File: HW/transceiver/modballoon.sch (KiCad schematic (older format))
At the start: 15 parts, among them K1 CONN_6, K2 CONN_10, K3 CONN_6, K4 CONN_6, K5 SMA, K6 SMA, K7 HE10-20

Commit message: PCB of transceiver designed.
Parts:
- added M1, M2, M3, M4: CONN_01X01, Balloln_pretty:M2, symbol CONN_01X01
- added M5, M6, M7, M8: CONN_01X01, Balloln_pretty:M3, symbol CONN_01X01
- added S1: BMI-S-210-F, Balloln_pretty:BMI-S-210-F, symbol CONN_01X24
- C1, C2: footprint ~ -> Capacitors_SMD:C_0603; symbol C -> C-RESCUE-modballoon
- DD1: footprint ~ -> TO_SOT_Packages_SMD:SC-70-5
- F1: footprint 0603 -> Resistors_SMD:R_0603
- K1, K3, K4: footprint (none) -> Pin_Headers:Pin_Header_Straight_1x06
- K2: footprint (none) -> Pin_Headers:Pin_Header_Straight_1x10
- K5, K6: footprint ~ -> Balloln_pretty:SMA
- K7: footprint (none) -> Pin_Headers:Pin_Header_Straight_2x10
- L1: footprint ~ -> Capacitors_SMD:C_0805
- R1, R2, R3: footprint ~ -> Resistors_SMD:R_0603; symbol R -> R-RESCUE-modballoon
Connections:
- net GND: now also M1.1 (P1), M2.1 (P1), M3.1 (P1), M4.1 (P1), M5.1 (P1), M6.1 (P1), M7.1 (P1), M8.1 (P1), S1.1 (P1), S1.10 (P10), S1.11 (P11), S1.12 (P12), S1.13 (P13), S1.14 (P14), S1.15 (P15), S1.16 (P16), S1.17 (P17), S1.18 (P18), S1.19 (P19), S1.2 (P2), S1.20 (P20), S1.21 (P21), S1.22 (P22), S1.23 (P23), S1.24 (P24), S1.3 (P3), S1.4 (P4), S1.5 (P5), S1.6 (P6), S1.7 (P7), S1.8 (P8), S1.9 (P9)

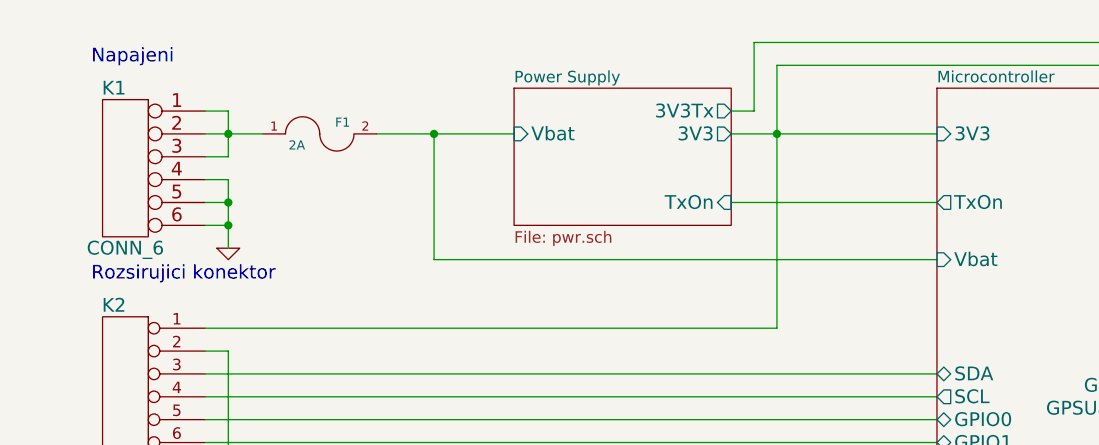
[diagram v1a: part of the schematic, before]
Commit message: new protection feature - inverted power supply protection diode.
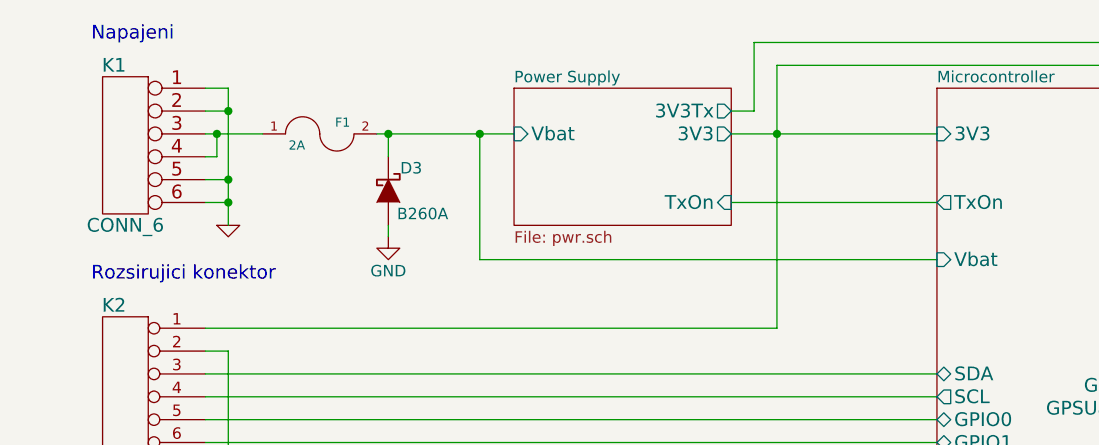
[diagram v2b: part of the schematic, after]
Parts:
- added D3: B260A, Diodes_SMD:SMA_Handsoldering, symbol D_Schottky
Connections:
- net GND: now also K1.1, K1.2, D3.2 (A); no longer K1.4
- net Microcontroller/Vbat: now also D3.1 (K)
- net at F1.1, K1.3: now also K1.4; no longer K1.1, K1.2
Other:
- moved on the sheet: K1
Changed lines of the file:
@@
 L CONN_6 K1
 U 1 1 57287BC9
-P 1200 2300
-F 0 "K1" H 1250 2650 60  0000 C CNN
-F 1 "CONN_6" H 1200 1950 60  0000 C CNN
-F 2 "Pin_Headers:Pin_Header_Straight_1x06" H 1200 2300 60  0001 C CNN
-F 3 "" H 1200 2300 60  0000 C CNN
-	1    1200 2300
+P 1200 2200
+F 0 "K1" H 1250 2550 60  0000 C CNN
+F 1 "CONN_6" H 1200 1850 60  0000 C CNN
+F 2 "Pin_Headers:Pin_Header_Straight_1x06" H 1200 2200 60  0001 C CNN
+F 3 "" H 1200 2200 60  0000 C CNN
+	1    1200 2200
 	-1   0    0    -1
 $EndComp
@@
 L GND-RESCUE-modballoon #PWR06
 U 1 1 5728802D
-P 1650 2650
-F 0 "#PWR06" H 1650 2650 30  0001 C CNN
-F 1 "GND" H 1650 2580 30  0001 C CNN
-F 2 "" H 1650 2650 60  0000 C CNN
-F 3 "" H 1650 2650 60  0000 C CNN
-	1    1650 2650
+P 1650 2550
+F 0 "#PWR06" H 1650 2550 30  0001 C CNN
+F 1 "GND" H 1650 2480 30  0001 C CNN
+F 2 "" H 1650 2550 60  0000 C CNN
+F 3 "" H 1650 2550 60  0000 C CNN
+	1    1650 2550
 	1    0    0    -1
 $EndComp
@@
 Text Notes 9450 2100 0    60   ~ 0
 Rx/Tx/1090MHz antena\n
-Text Notes 1050 1850 0    60   ~ 0
+Text Notes 1050 1750 0    60   ~ 0
 Napajeni\n
 Text Notes 1050 2800 0    60   ~ 0
@@
 Connection ~ 7350 3250
 Wire Wire Line
-	2550 2150 2550 2700
-Connection ~ 2550 2150
+	2750 2150 2750 2700
+Connection ~ 2750 2150
 Wire Wire Line
 	9800 4000 9650 4000
@@
 	7000 5550 7950 5550
 Wire Wire Line
-	2550 2700 4750 2700
-Wire Wire Line
-	1550 2050 1650 2050
-Wire Wire Line
-	1650 2050 1650 2250
-Wire Wire Line
-	1650 2250 1550 2250
-Wire Wire Line
-	1550 2150 1800 2150
-Connection ~ 1650 2150
-Wire Wire Line
-	1550 2350 1650 2350
-Wire Wire Line
-	1650 2350 1650 2650
-Wire Wire Line
-	1550 2550 1650 2550
-Connection ~ 1650 2550
+	2750 2700 4750 2700
+Wire Wire Line
+	1550 1950 1650 1950
+Connection ~ 1650 2050
 Wire Wire Line
 	1550 2450 1650 2450
 Connection ~ 1650 2450
+Wire Wire Line
+	1550 2350 1650 2350
+Connection ~ 1650 2350
 Wire Wire Line
 	1650 3100 1650 4000
@@
 Wire Wire Line
 	1800 7400 1800 7300
+$Comp
+L D_Schottky D3
+U 1 1 57CEBDCD
+P 2350 2400
+F 0 "D3" V 2250 2500 50  0000 C CNN
+F 1 "B260A" V 2450 2550 50  0000 C CNN
+F 2 "Diodes_SMD:SMA_Handsoldering" H 2350 2400 50  0001 C CNN
+F 3 "" H 2350 2400 50  0000 C CNN
+	1    2350 2400
+	0    1    1    0
+$EndComp
+$Comp
+L GND #PWR020
+U 1 1 57CEBFFC
+P 2350 2600
+F 0 "#PWR020" H 2350 2350 50  0001 C CNN
+F 1 "GND" H 2350 2450 50  0000 C CNN
+F 2 "" H 2350 2600 50  0000 C CNN
+F 3 "" H 2350 2600 50  0000 C CNN
+	1    2350 2600
+	1    0    0    -1
+$EndComp
+Wire Wire Line
+	2350 2250 2350 2150
+Connection ~ 2350 2150
+Wire Wire Line
+	2350 2550 2350 2600
+Wire Wire Line
+	1650 1950 1650 2550
+Wire Wire Line
+	1550 2050 1650 2050
+Wire Wire Line
+	1550 2250 1600 2250
+Wire Wire Line
+	1600 2250 1600 2150
+Wire Wire Line
+	1550 2150 1800 2150
+Connection ~ 1600 2150
 $EndSCHEMATC
